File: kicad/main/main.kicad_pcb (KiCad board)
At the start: 2 copper layers, 147 parts, among them J1 USB2.0_C_v3, J10 MD2, J11 Drib, J12 SW1, J13 I2C_1, J14 drib-kick, J15 drib-kick, J16 I2C_2, J17 5V OUT, J18 LINE, J19 SW1, J2 AUX1, J20 ICSP, J21 MD1, J22 MD2, J23 MD3, J24 MD4, J25 I2C/OLED, J26 ICSP, J27 Trimmer, J3 I2C_3, J4 XBee, J5 Serial3/OpenMV, J6 Power IN, J7 LED, J8 Kicker, J9 MD1, Q1 AO3400A, Q2 AO3401A, SW1 Reset, SW2 GOAL, SW3 START, SW4 AUX1, SW5 IMU SET, SW6 RESET, SW7 BOOTSEL, U1 AZ1117CH-3.3, U10 W25Q128JVS, U2 74HC32, U3 74HC04, U4 OKL-T_3-W12N-C, U5 PCF8574PW, U6 AE-BNO055, U7 ATmega328P-AU, U8 ATmega328P-AU, U9 RP2040, Y1 8Mhz, Y2 8Mhz, Y3 12Mhz

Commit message: no message
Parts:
- removed J10: MD2, Connector_JST:JST_XH_S2B-XH-A-1_1x02_P2.50mm_Horizontal
- removed J25: I2C/OLED, 0.main.robot:JSTB4B-ZR
- removed J26: ICSP, 0.main.robot:JSTB6B-ZR
- removed J27: Trimmer, 0.main.robot:JSTS6B-ZRLFSN
- removed J7: LED, 0.main.robot:JSTB6B-ZR
- removed JP2: SolderJumper_2_Open, Jumper:SolderJumper-2_P1.3mm_Open_RoundedPad1.0x1.5mm
- removed JP3: Jumper_2_Bridged, Connector_PinHeader_1.27mm:PinHeader_1x02_P1.27mm_Vertical
- removed R49: 1kR, Resistor_SMD:R_0603_1608Metric_Pad0.98x0.95mm_HandSolder
- added C26: 0.1u, Capacitor_SMD:C_0603_1608Metric_Pad1.08x0.95mm_HandSolder, F.Cu at (170.0, 125.0)
- added C27: 10u, Capacitor_SMD:C_0603_1608Metric_Pad1.08x0.95mm_HandSolder, B.Cu at (128.0, 102.1)
- added D17: RSX101VAM-30, Diode_SMD:D_0805_2012Metric_Pad1.15x1.40mm_HandSolder, F.Cu at (142.0, 120.0)
- added D18: LED(OSWT1608), 0.main.robot:LED_SMLE13WBC8W1, F.Cu at (125.0, 103.1)
- added U11: AE-BNO055, 0.main.robot:AE-BNO055, F.Cu at (135.0, 127.0)
- C10: value 10u -> 0.1u
- C11, C12, C15, C16, C17, C22, C23, C3, C6, C8, D1, D2, D3, J1, R3, R40, SW1, U3, U4, Y2: moved to B.Cu
- C13: value 10u -> 0.1u; moved to B.Cu
- C14, C19: value 0.1u -> 1uF; moved to B.Cu
- C18, C21: value 1uF -> 0.1u; moved to B.Cu
- C24, C25: value 0.1u -> 10uF; moved to B.Cu
- C9: value 0.1u -> 10u
- D10: value RSX101VAM-30TR -> RSX101VAM-30
- D11, D12: value LED(OSWT1608) -> RSX101VAM-30; footprint LED_SMD:LED_0603_1608Metric_Pad1.05x0.95mm_HandSolder -> Diode_SMD:D_0805_2012Metric_Pad1.15x1.40mm_HandSolder; moved to B.Cu
- D13: value RSX101VAM-30TR -> LED1_R; footprint Diode_SMD:D_0805_2012Metric_Pad1.15x1.40mm_HandSolder -> 0.main.robot:LED_SMLE13WBC8W1
- D14: value LED(OSWT1608) -> LED2_G
- D15: value RSX101VAM-30 -> LED3_Y; footprint Diode_SMD:D_0805_2012Metric_Pad1.15x1.40mm_HandSolder -> 0.main.robot:LED_SMLE13WBC8W1
- D16: value RSX101VAM-30 -> LED4_B; footprint Diode_SMD:D_0805_2012Metric_Pad1.15x1.40mm_HandSolder -> 0.main.robot:LED_SMLE13WBC8W1
- D5: value LED1_R -> RSX101VAM-30TR; footprint 0.main.robot:LED_SMLE13WBC8W1 -> Diode_SMD:D_0805_2012Metric_Pad1.15x1.40mm_HandSolder
- D6: value LED2_G -> LED(OSWT1608); footprint 0.main.robot:LED_SMLE13WBC8W1 -> LED_SMD:LED_0603_1608Metric_Pad1.05x0.95mm_HandSolder
- D7: value LED3_Y -> LED(OSWT1608); footprint 0.main.robot:LED_SMLE13WBC8W1 -> LED_SMD:LED_0603_1608Metric_Pad1.05x0.95mm_HandSolder
- D8: value LED4_B -> RSX101VAM-30TR; footprint 0.main.robot:LED_SMLE13WBC8W1 -> Diode_SMD:D_0805_2012Metric_Pad1.15x1.40mm_HandSolder
- J11: value Drib -> I2C_1; footprint Connector_JST:JST_XH_B2B-XH-A_1x02_P2.50mm_Vertical -> 0.main.robot:JSTB4B-ZR
- J12: value SW1 -> drib-kick; footprint 0.main.robot:JSTB6B-ZR -> Connector_PinHeader_2.54mm:PinHeader_1x04_P2.54mm_Vertical; moved to B.Cu
- J13: value I2C_1 -> drib-kick; footprint 0.main.robot:JSTB4B-ZR -> Connector_PinHeader_2.54mm:PinHeader_1x04_P2.54mm_Vertical; moved to B.Cu
- J14: value drib-kick -> I2C_2
- J15: value drib-kick -> 5V OUT; footprint 0.main.robot:JSTB4B-ZR -> Connector_JST:JST_XH_B2B-XH-A_1x02_P2.50mm_Vertical
- J16: value I2C_2 -> LINE; footprint 0.main.robot:JSTB4B-ZR -> 0.main.robot:JSTB8B-ZR
- J17: value 5V OUT -> ICSP; footprint Connector_JST:JST_XH_B2B-XH-A_1x02_P2.50mm_Vertical -> 0.main.robot:JSTB6B-ZR
- J18: value LINE -> MD1; footprint 0.main.robot:JSTB8B-ZR -> 0.main.robot:JSTB4B-ZR
- J19: value SW1 -> MD2; footprint 0.main.robot:JSTS6B-ZRLFSN -> 0.main.robot:JSTB4B-ZR
- J20: value ICSP -> MD3; footprint 0.main.robot:JSTB6B-ZR -> 0.main.robot:JSTB4B-ZR
- J21: value MD1 -> MD4
- J22: value MD2 -> I2C/OLED
- J23: value MD3 -> ICSP; footprint 0.main.robot:JSTB4B-ZR -> 0.main.robot:JSTB6B-ZR
- J24: value MD4 -> Trimmer; footprint 0.main.robot:JSTB4B-ZR -> 0.main.robot:JSTB6B-ZR
- J4: footprint 0.main.robot:JSTB4B-ZR -> Connector_PinHeader_2.54mm:PinHeader_1x04_P2.54mm_Vertical; moved to B.Cu
- J5: value Serial3/OpenMV -> Power IN; footprint 0.main.robot:JSTB4B-ZR -> Connector_JST:JST_VH_B2P-VH-B_1x02_P3.96mm_Vertical
- J6: value Power IN -> Serial3/OpenMV; footprint Connector_JST:JST_VH_B2P-VH-B_1x02_P3.96mm_Vertical -> 0.main.robot:JSTB4B-ZR
- J8: value Kicker -> MD1; footprint Connector_JST:JST_XH_B2B-XH-A_1x02_P2.50mm_Vertical -> Connector_JST:JST_XH_S2B-XH-A-1_1x02_P2.50mm_Horizontal
- J9: value MD1 -> MD2
- JP1: value SolderJumper_2_Open -> Jumper_2_Bridged; footprint Jumper:SolderJumper-2_P1.3mm_Open_RoundedPad1.0x1.5mm -> Connector_PinHeader_1.27mm:PinHeader_1x02_P1.27mm_Vertical
- R11: value 1k -> 330
- R13: value 330 -> 10k; footprint Resistor_THT:R_Axial_DIN0204_L3.6mm_D1.6mm_P5.08mm_Horizontal -> Resistor_SMD:R_0603_1608Metric_Pad0.98x0.95mm_HandSolder
- R16, R4: value 47k -> 10k
- R17, R5, R6: value 10k -> 47k; moved to B.Cu
- R18: value 470 -> 10k; moved to B.Cu
- R19: value 470 -> 47k
- R20, R23, R28: value 47k -> 470
- R24: value 120 -> 10k
- R25, R26, R27: value 120 -> 47k; moved to B.Cu
- R29: value 47k -> 10k; moved to B.Cu
- R30: value 470 -> 1k
- R31: value 47k -> 200R
- R32: value 470 -> 1R
- R33, R34: value 47k -> 27.4R
- R35: value 470 -> 10kR; moved to B.Cu
- R36: value 10k -> 1kR
- R37: value 47k -> 470; moved to B.Cu
- R41, R7: value 10k -> 47k
- R42, R43: value 1k -> 120
- R44: value 200R -> 120
- R45: value 1R -> 120
- R46, R47: value 27.4R -> 47k; moved to B.Cu
- R48: value 10kR -> 470; moved to B.Cu
- R9: value 10k -> 1k; footprint Resistor_SMD:R_0603_1608Metric_Pad0.98x0.95mm_HandSolder -> Resistor_THT:R_Axial_DIN0204_L3.6mm_D1.6mm_P5.08mm_Horizontal
- SW2: value GOAL -> RESET; footprint 0.main.robot:MFS101D-14-Z -> 0.main.robot:TVAF06-A020B-R; moved to B.Cu
- SW3: value START -> BOOTSEL; footprint 0.main.robot:SW_NKK_B-12CCPRM -> 0.main.robot:TVAF06-A020B-R; moved to B.Cu
- SW4: value AUX1 -> IMU SET; footprint Button_Switch_THT:SW_DIP_SPSTx02_Slide_9.78x7.26mm_W7.62mm_P2.54mm -> Button_Switch_THT:SW_Tactile_Straight_KSA0Axx1LFTR
- SW5: value IMU SET -> GOAL; footprint 0.main.robot:TVAF06-A020B-R -> 0.main.robot:MFS101D-14-Z
- SW6: value RESET -> START; footprint 0.main.robot:TVAF06-A020B-R -> 0.main.robot:SW_NKK_B-12CCPRM
- SW7: value BOOTSEL -> AUX1; footprint 0.main.robot:TVAF06-A020B-R -> Button_Switch_THT:SW_DIP_SPSTx02_Slide_9.78x7.26mm_W7.62mm_P2.54mm
- U10: value W25Q128JVS -> PCF8574PW; footprint rp2040:W25Q16-128JV-SOIC -> Package_SO:TSSOP-20_4.4x6.5mm_P0.65mm; moved to B.Cu
- U5: value PCF8574PW -> ATmega328P-AU; footprint Package_SO:TSSOP-20_4.4x6.5mm_P0.65mm -> Package_QFP:TQFP-32_7x7mm_P0.8mm
- U6: value AE-BNO055 -> ATmega328P-AU; footprint 0.main.robot:AE-BNO055 -> Package_QFP:TQFP-32_7x7mm_P0.8mm
- U7: value ATmega328P-AU -> RP2040; footprint Package_QFP:TQFP-32_7x7mm_P0.8mm -> rp2040:RP2040_hand
- U8: value ATmega328P-AU -> W25Q128JVS; footprint Package_QFP:TQFP-32_7x7mm_P0.8mm -> rp2040:W25Q16-128JV-SOIC; moved to B.Cu
- U9: value RP2040 -> AZ1117CH-3.3; footprint rp2040:RP2040_hand -> Package_TO_SOT_SMD:SOT-223-3_TabPin2
- Y1, Y3: footprint Crystal:Resonator_SMD_Murata_CSTxExxV-3Pin_3.0x1.1mm_HandSoldering -> Crystal:Resonator-3Pin_W6.0mm_H3.0mm; moved to B.Cu
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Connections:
- C1 pad 2: GND -> SW1_6
- C10 pad 1: Net-(C10-Pad1) -> Vcc1
- C10 pad 2: GND -> SW1_6
- C11 pad 1: Vcc1 -> Net-(C11-Pad1)
- C11 pad 2: GND -> SW1_6
- C12 pad 1: Vcc1 -> +1V1
- C12 pad 2: GND -> SW1_6
- C13 pad 1: RESET -> +1V1
- C13 pad 2: GND -> SW1_6
- C14 pad 2: GND -> SW1_6
- C15 pad 1: +1V1 -> SW1_3
- C15 pad 2: GND -> SW1_6
- C16 pad 1: +1V1 -> SW1_3
- C16 pad 2: GND -> SW1_6
- C17 pad 1: +3V3 -> SW1_3
- C17 pad 2: GND -> SW1_6
- C18 pad 1: +3V3 -> SW1_3
- C18 pad 2: GND -> SW1_6
- C19 pad 1: +3V3 -> Net-(C19-Pad1)
- C19 pad 2: GND -> SW1_6
- C2 pad 1: +3V3 -> SW1_3
- C2 pad 2: GND -> SW1_6
- C20 pad 1: +3V3 -> SW1_3
- C20 pad 2: GND -> SW1_6
- C21 pad 1: Net-(C21-Pad1) -> SW1_3
- C21 pad 2: GND -> SW1_6
- C22 pad 1: +3V3 -> SW1_3
- C22 pad 2: GND -> SW1_6
- C23 pad 1: +3V3 -> SW1_3
- C23 pad 2: GND -> SW1_6
- C24 pad 1: +3V3 -> +5V
- C24 pad 2: GND -> SW1_6
- C25 pad 1: +3V3 -> Net-(C25-Pad1)
- C25 pad 2: GND -> SW1_6
- C3 pad 1: GND -> SW1_6
- C3 pad 2: /rp2040/RUN(RES)/30 -> RESET
- C4 pad 2: GND -> SW1_6
- C5 pad 2: Net-(C5-Pad2) -> SW1_6
- C6 pad 2: GND -> SW1_6
- C7 pad 1: +3V3 -> +3.3VA
- C7 pad 2: GND -> SW1_6
- C8 pad 1: +3V3 -> Net-(C8-Pad1)
- C8 pad 2: GND -> SW1_6
- C9 pad 1: +3.3VA -> Vcc1
- C9 pad 2: GND -> SW1_6
- D10 pad 1: +3.3VA -> RESET
- D10 pad 2: +3V3 -> Net-(C11-Pad1)
- D11 pad 1: GND -> Vcc1
- D11 pad 2: Net-(D11-Pad2) -> Net-(C11-Pad1)
- D12 pad 1: GND -> Vcc1
- D13 pad 1: +3.3VA -> Net-(D13-Pad1)
- D13 pad 2: Net-(C10-Pad1) -> Net-(D13-Pad2)
- D14 pad 1: GND -> Net-(D14-Pad1)
- D14 pad 2: Net-(D14-Pad2) -> Net-(D13-Pad2)
- D15 pad 1: Vcc1 -> Net-(D15-Pad1)
- D15 pad 2: RESET -> Net-(D13-Pad2)
- D16 pad 1: Vcc1 -> Net-(D16-Pad1)
- D16 pad 2: Net-(D16-Pad2) -> Net-(D13-Pad2)
- D3 pad 1: +3V3 -> SW1_3
- D3 pad 2: /rp2040/RUN(RES)/30 -> RESET
- D4 pad 1: GND -> SW1_6
- D5 pad 1: Net-(D5-Pad1) -> +3.3VA
- D5 pad 2: Net-(D5-Pad2) -> SW1_3
- D6 pad 1: Net-(D5-Pad1) -> SW1_6
- D7 pad 1: Net-(D5-Pad1) -> SW1_6
- D8 pad 1: Net-(D5-Pad1) -> +3.3VA
- D8 pad 2: Net-(D8-Pad2) -> Net-(C8-Pad1)
- D9 pad 1: GND -> SW1_6
- J1 pad 4: GND -> SW1_6
- J11 pad 1: +15V -> SCL_IMU
- J11 pad 2: GND -> SW1_3
- J12 pad 1: /rp2040/GPIO03/05 -> /rp2040/GPIO13/17
- J12 pad 2: /rp2040/GPIO06/09 -> SW1_6
- J12 pad 3: +3V3 -> /rp2040/GPIO12/16
- J12 pad 4: /rp2040/GPIO02/04 -> SW1_6
- J13 pad 1: SCL_IMU -> +15V
- J13 pad 2: +3V3 -> SW1_6
- J13 pad 3: SDA_IMU -> +15V
- J13 pad 4: GND -> SW1_6
- J14 pad 1: /rp2040/GPIO13/17 -> SCL_IMU
- J14 pad 2: GND -> SW1_3
- J14 pad 3: /rp2040/GPIO12/16 -> SDA_IMU
- J14 pad 4: GND -> SW1_6
- J15 pad 1: +15V -> +5V
- J15 pad 2: GND -> SW1_6
- J16 pad 1: SCL_IMU -> Net-(J16-Pad1)
- J16 pad 2: +3V3 -> Net-(J16-Pad2)
- J16 pad 3: SDA_IMU -> Net-(J16-Pad3)
- J16 pad 4: GND -> Net-(J16-Pad4)
- J17 pad 2: Net-(C5-Pad2) -> +3.3VA
- J18 pad 1: Net-(J18-Pad1) -> Net-(J17-Pad4)
- J18 pad 2: Net-(J18-Pad2) -> Net-(J17-Pad1)
- J18 pad 3: Net-(J18-Pad3) -> Net-(J17-Pad4)
- J18 pad 4: Net-(J18-Pad4) -> Net-(J17-Pad3)
- J19 pad 3: Net-(J19-Pad3) -> Net-(J19-Pad1)
- J2 pad 2: +3V3 -> SW1_3
- J2 pad 4: GND -> SW1_6
- J20 pad 2: +3.3VA -> Net-(J20-Pad2)
- J20 pad 3: Net-(J20-Pad3) -> Net-(J20-Pad1)
- J21 pad 1: Net-(J20-Pad4) -> Net-(J21-Pad1)
- J21 pad 2: Net-(J20-Pad1) -> Net-(J21-Pad2)
- J21 pad 3: Net-(J20-Pad4) -> Net-(J21-Pad1)
- J21 pad 4: Net-(J20-Pad3) -> Net-(J21-Pad4)
- J22 pad 1: Net-(J22-Pad1) -> /LineTrimmer/SCL
- J22 pad 2: Net-(J22-Pad2) -> Vcc1
- J22 pad 3: Net-(J22-Pad1) -> /LineTrimmer/SDA
- J22 pad 4: Net-(J22-Pad4) -> SW1_6
- J23 pad 2: Net-(J23-Pad2) -> Vcc1
- J23 pad 3: Net-(J23-Pad1) -> Net-(J23-Pad3)
- J24 pad 3: Net-(J24-Pad1) -> Net-(J24-Pad3)
- J3 pad 2: +3V3 -> SW1_3
- J3 pad 4: GND -> SW1_6
- J4 pad 3: /rp2040/GPIO01/02 -> Net-(J4-Pad3)
- J4 pad 4: GND -> SW1_6
- J5 pad 1: /rp2040/GPIO08/11 -> SW1_6
- J5 pad 2: +5V -> +15V
- J6 pad 1: GND -> /rp2040/GPIO08/11
- J6 pad 2: +15V -> +5V
- J8 pad 1: +15V -> SW1_6
- J8 pad 2: GND -> +15V
- J9 pad 1: GND -> SW1_6
- JP1 pad 1: Net-(JP1-Pad1) -> Net-(C25-Pad1)
- JP1 pad 2: Net-(J19-Pad5) -> Net-(D13-Pad2)
- Q1 pad 2: GND -> SW1_6
- Q2 pad 3: Net-(J18-Pad4) -> Net-(J16-Pad4)
- R1 pad 2: GND -> SW1_6
- R10 pad 2: Net-(J18-Pad6) -> Net-(J16-Pad2)
- R11 pad 1: Net-(R11-Pad1) -> SW1_6
- R12 pad 2: Net-(J18-Pad3) -> Net-(J16-Pad5)
- R13 pad 1: GND -> Net-(R13-Pad1)
- R13 pad 2: Net-(R11-Pad1) -> Net-(J16-Pad6)
- R14 pad 1: +5V -> Net-(R14-Pad1)
- R14 pad 2: Net-(Q1-Pad3) -> Net-(J16-Pad3)
- R15 pad 1: Net-(J17-Pad1) -> +5V
- R16 pad 1: +15V -> +5V
- R16 pad 2: Vbatt -> Net-(Q1-Pad3)
- R17 pad 1: Vbatt -> +15V
- R17 pad 2: GND -> Vbatt
- R18 pad 1: Net-(J19-Pad2) -> Vbatt
- R18 pad 2: Net-(R18-Pad2) -> SW1_6
- R19 pad 1: Net-(J19-Pad5) -> Net-(R19-Pad1)
- R19 pad 2: Net-(R19-Pad2) -> +3.3VA
- R2 pad 2: GND -> SW1_6
- R20 pad 1: +3V3 -> +3.3VA
- R20 pad 2: Net-(R20-Pad2) -> Net-(D6-Pad2)
- R21 pad 1: +3V3 -> +3.3VA
- R21 pad 2: Net-(R21-Pad2) -> /Sheet63625160/SCL_1
- R22 pad 1: +3V3 -> +3.3VA
- R22 pad 2: Net-(R22-Pad2) -> /Sheet63625160/SDA_1
- R23 pad 1: +3V3 -> Net-(R23-Pad1)
- R23 pad 2: Net-(R23-Pad2) -> Net-(D7-Pad2)
- R24 pad 1: Net-(R24-Pad1) -> Net-(C8-Pad1)
- R24 pad 2: Net-(D5-Pad2) -> +3.3VA
- R25 pad 2: Net-(D6-Pad2) -> Vcc1
- R26 pad 1: Net-(R26-Pad1) -> Vcc1
- R26 pad 2: Net-(D7-Pad2) -> /LineTrimmer/SCL
- R27 pad 1: Net-(JP2-Pad1) -> Vcc1
- R27 pad 2: Net-(D8-Pad2) -> /LineTrimmer/SDA
- R28 pad 1: +3V3 -> Net-(R28-Pad1)
- R28 pad 2: SDA_IMU -> Net-(D9-Pad2)
- R29 pad 1: +3V3 -> Net-(C11-Pad1)
- R29 pad 2: SCL_IMU -> Vcc1
- R3 pad 1: /rp2040/GPIO09/12 -> /rp2040/GPIO01/02
- R3 pad 2: Net-(J5-Pad3) -> Net-(J4-Pad3)
- R30 pad 1: +3V3 -> Net-(R30-Pad1)
- R30 pad 2: Net-(D9-Pad2) -> Net-(R30-Pad2)
- R31 pad 1: Net-(R31-Pad1) -> ADC_VREF
- R31 pad 2: +3.3VA -> SW1_3
- R32 pad 1: +3.3VA -> Net-(C19-Pad1)
- R32 pad 2: Net-(D11-Pad2) -> ADC_VREF
- R33 pad 1: +3.3VA -> Net-(R33-Pad1)
- R33 pad 2: /Sheet63625160/SCL_1 -> USB_DP
- R34 pad 1: +3.3VA -> Net-(R34-Pad1)
- R34 pad 2: /Sheet63625160/SDA_1 -> USB_DM
- R35 pad 1: Net-(R35-Pad1) -> QSPI_SS
- R35 pad 2: Net-(D12-Pad2) -> SW1_3
- R36 pad 1: Net-(C10-Pad1) -> Net-(R36-Pad1)
- R36 pad 2: +3.3VA -> QSPI_SS
- R37 pad 2: Vcc1 -> Net-(R37-Pad2)
- R38 pad 1: Vcc1 -> Net-(C25-Pad1)
- R38 pad 2: /LineTrimmer/SCL -> Net-(R38-Pad2)
- R39 pad 1: Vcc1 -> Net-(C25-Pad1)
- R39 pad 2: /LineTrimmer/SDA -> Net-(R39-Pad2)
- R4 pad 1: +3V3 -> /rp2040/GPIO09/12
- R4 pad 2: /rp2040/RUN(RES)/30 -> Net-(J6-Pad3)
- R40 pad 2: Net-(D14-Pad2) -> Net-(R40-Pad2)
- R41 pad 1: RESET -> Net-(C25-Pad1)
- R41 pad 2: Vcc1 -> Net-(R41-Pad2)
- R42 pad 1: /rp2040/RUN(RES)/30 -> Net-(R42-Pad1)
- R42 pad 2: +3V3 -> Net-(D13-Pad1)
- R43 pad 2: Net-(R43-Pad2) -> Net-(D14-Pad1)
- R44 pad 1: ADC_VREF -> Net-(R44-Pad1)
- R44 pad 2: +3V3 -> Net-(D15-Pad1)
- R45 pad 1: Net-(C21-Pad1) -> Net-(R45-Pad1)
- R45 pad 2: ADC_VREF -> Net-(D16-Pad1)
- R46 pad 1: Net-(R46-Pad1) -> Net-(C25-Pad1)
- R46 pad 2: USB_DP -> SDA_IMU
- R47 pad 1: Net-(R47-Pad1) -> Net-(C25-Pad1)
- R47 pad 2: USB_DM -> SCL_IMU
- R48 pad 1: QSPI_SS -> Net-(C25-Pad1)
- R48 pad 2: +3V3 -> Net-(D18-Pad2)
- R5 pad 1: +3V3 -> SW1_3
- R5 pad 2: SCL_IMU -> RESET
- R6 pad 1: +3V3 -> SW1_3
- R6 pad 2: SDA_IMU -> SCL_IMU
- R7 pad 1: Net-(R7-Pad1) -> SW1_3
- R7 pad 2: Net-(J18-Pad1) -> SDA_IMU
- R8 pad 2: Net-(J18-Pad2) -> Net-(J16-Pad1)
- R9 pad 1: Net-(R9-Pad1) -> Net-(R11-Pad2)
- R9 pad 2: Net-(J18-Pad5) -> Net-(R9-Pad2)
- RV1 pad 1: Net-(D16-Pad2) -> Net-(D12-Pad2)
- RV1 pad 2: Net-(J27-Pad1) -> Net-(J24-Pad1)
- RV1 pad 3: Net-(J27-Pad1) -> Net-(J24-Pad1)
- RV2 pad 1: Net-(D16-Pad2) -> Net-(D12-Pad2)
- RV2 pad 2: Net-(J27-Pad2) -> Net-(J24-Pad2)
- RV2 pad 3: Net-(J27-Pad2) -> Net-(J24-Pad2)
- RV3 pad 1: Net-(D16-Pad2) -> Net-(D12-Pad2)
- RV3 pad 2: Net-(J27-Pad3) -> Net-(J24-Pad3)
- RV3 pad 3: Net-(J27-Pad3) -> Net-(J24-Pad3)
- RV4 pad 1: Net-(D16-Pad2) -> Net-(D12-Pad2)
- RV4 pad 2: Net-(J27-Pad4) -> Net-(J24-Pad4)
- RV4 pad 3: Net-(J27-Pad4) -> Net-(J24-Pad4)
- RV5 pad 1: Net-(D16-Pad2) -> Net-(D12-Pad2)
- SW1 pad 1: /rp2040/RUN(RES)/30 -> RESET
- SW1 pad 2: GND -> SW1_6
- SW2 pad 1: Net-(J19-Pad3) -> SW1_6
- SW2 pad 2: Net-(J19-Pad1) -> Net-(C11-Pad1)
- SW3 pad 1: Net-(J19-Pad3) -> SW1_6
- SW3 pad 2: Net-(J19-Pad4) -> Net-(R36-Pad1)
- SW4 pad 1: GND -> SW1_5
- SW4 pad 2: GND -> SW1_6
- SW5 pad 1: Net-(R22-Pad2) -> SW1_3
- SW5 pad 2: GND -> SW1_1
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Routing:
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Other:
- board outline added: 169.8 x 107.5 mm

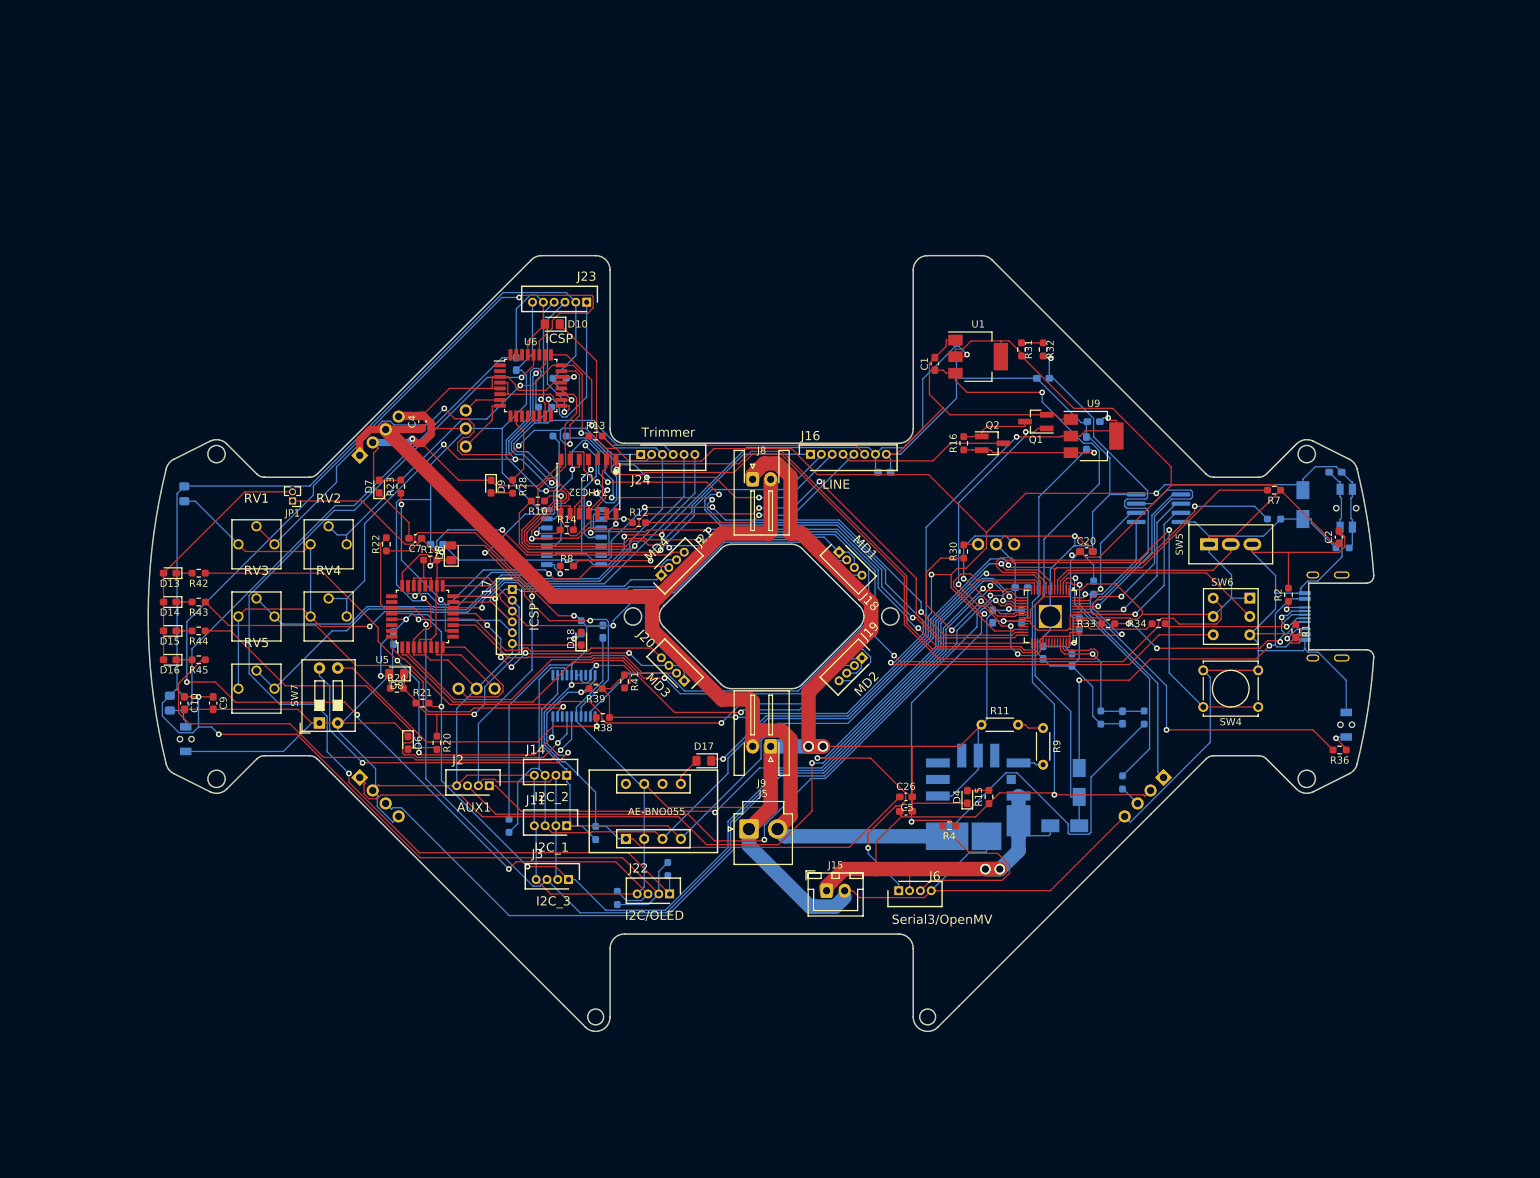
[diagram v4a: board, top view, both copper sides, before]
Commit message: fix: vison-board GND
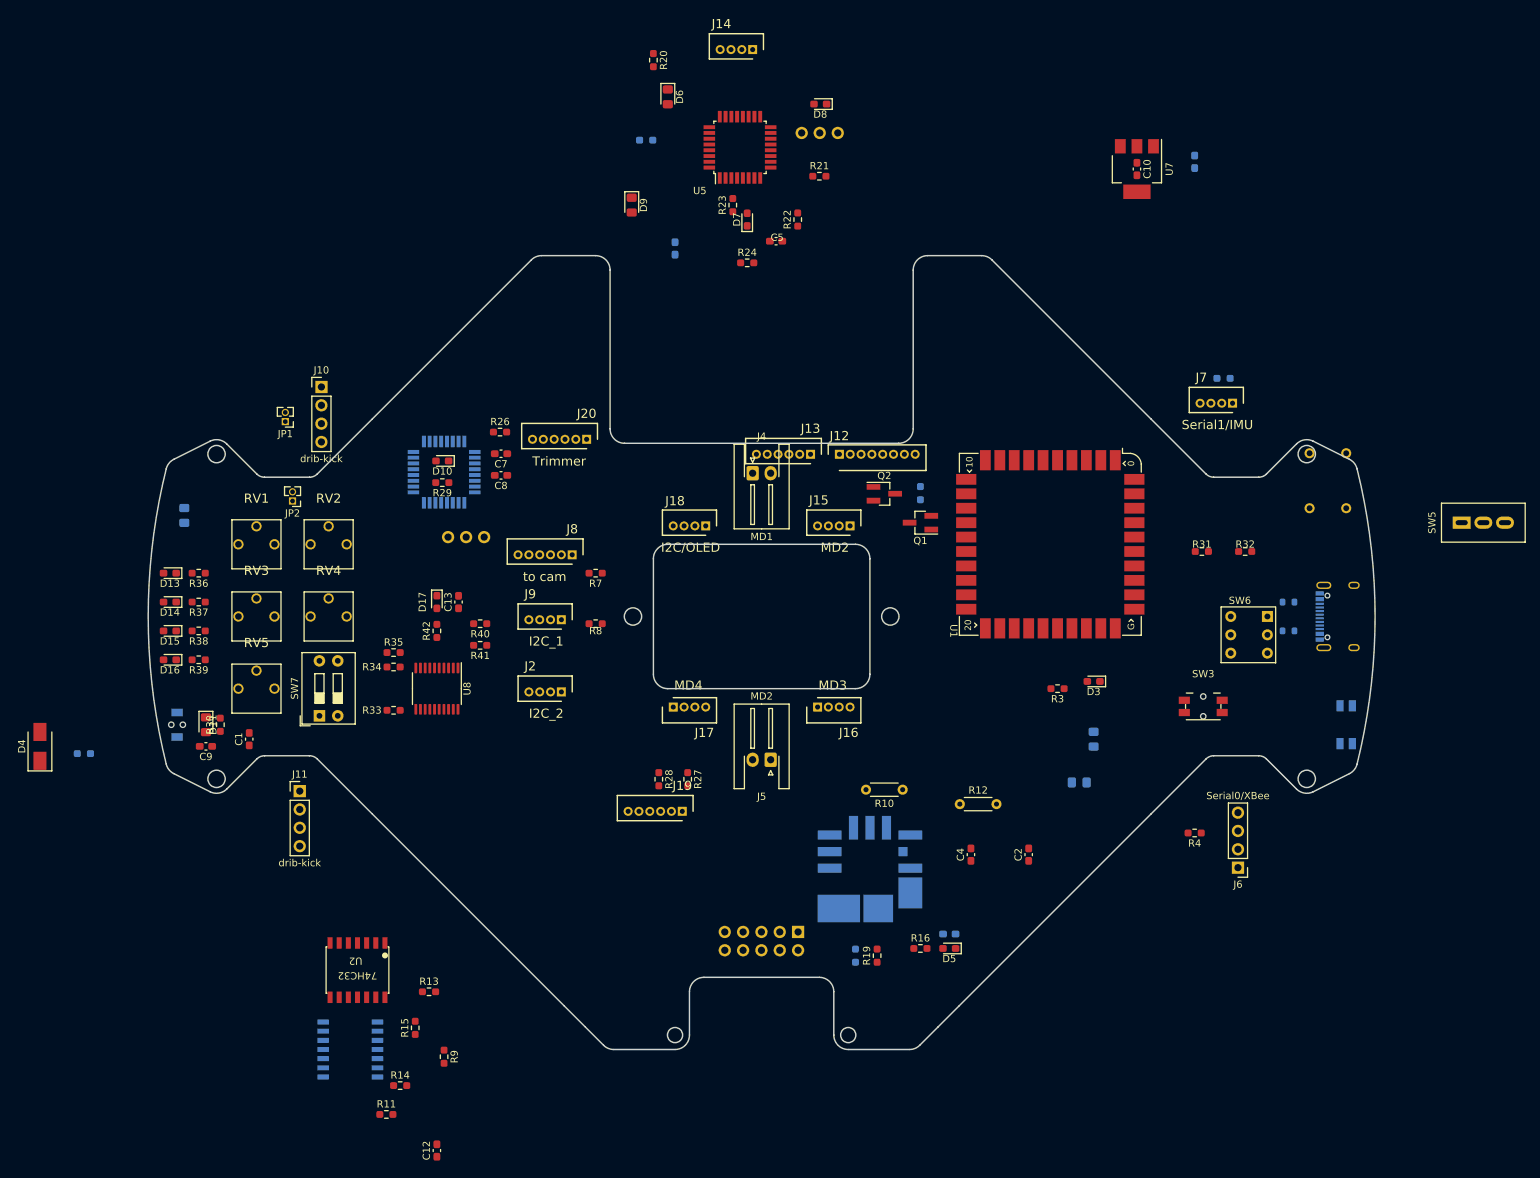
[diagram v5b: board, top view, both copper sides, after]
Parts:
- removed C14, C16, C19: 1uF, Capacitor_SMD:C_0603_1608Metric_Pad1.08x0.95mm_HandSolder
- removed C15, C17, C18, C20, C21, C22, C23, C26: 0.1u, Capacitor_SMD:C_0603_1608Metric_Pad1.08x0.95mm_HandSolder
- removed C24, C25: 10uF, Capacitor_SMD:C_0603_1608Metric_Pad1.08x0.95mm_HandSolder
- removed C27: 10u, Capacitor_SMD:C_0603_1608Metric_Pad1.08x0.95mm_HandSolder
- removed D18: LED(OSWT1608), 0.main.robot:LED_SMLE13WBC8W1
- removed J21: MD4, 0.main.robot:JSTB4B-ZR
- removed J22: I2C/OLED, 0.main.robot:JSTB4B-ZR
- removed J23: ICSP, 0.main.robot:JSTB6B-ZR
- removed J24: Trimmer, 0.main.robot:JSTB6B-ZR
- removed R43, R44, R45: 120, Resistor_SMD:R_0603_1608Metric_Pad0.98x0.95mm_HandSolder
- removed R46, R47: 47k, Resistor_SMD:R_0603_1608Metric_Pad0.98x0.95mm_HandSolder
- removed R48: 470, Resistor_SMD:R_0603_1608Metric_Pad0.98x0.95mm_HandSolder
- removed U10: PCF8574PW, Package_SO:TSSOP-20_4.4x6.5mm_P0.65mm
- removed U11: AE-BNO055, 0.main.robot:AE-BNO055
- removed U9: AZ1117CH-3.3, Package_TO_SOT_SMD:SOT-223-3_TabPin2
- removed Y3: 12Mhz, Crystal:Resonator-3Pin_W6.0mm_H3.0mm
- added J10: drib-kick, Connector_PinHeader_2.54mm:PinHeader_1x04_P2.54mm_Vertical, F.Cu at (89.0, 68.2)
- added J7: Serial1/IMU, 0.main.robot:JSTB4B-ZR, F.Cu at (215.2, 70.5)
- added JP2: Jumper_2_Bridged, Connector_PinHeader_1.27mm:PinHeader_1x02_P1.27mm_Vertical, F.Cu at (85.0, 84.0)
- C1, C2: value 10uF -> 10u
- C10: value 0.1u -> 10uF
- C11: value 10u -> 10uF
- C12, D11, R26: moved to F.Cu
- C13: value 0.1u -> 10u; moved to F.Cu
- C5: value 10u -> 0.1u
- C7: value 0.1u -> 10u
- C8: value 10u -> 0.1u; moved to F.Cu
- D1, D2: value SX34F -> D_Schottky; footprint Diode_SMD:D_SMA -> Diode_SMD:D_0805_2012Metric_Pad1.15x1.40mm_HandSolder
- D10, D17: value RSX101VAM-30 -> LED(OSWT1608); footprint Diode_SMD:D_0805_2012Metric_Pad1.15x1.40mm_HandSolder -> 0.main.robot:LED_SMLE13WBC8W1
- D3: value RSX101VAM-30TR -> LED; footprint Diode_SMD:D_SMA -> 0.main.robot:LED_SMLE13WBC8W1; moved to F.Cu
- D4: value LED -> RSX101VAM-30TR; footprint 0.main.robot:LED_SMLE13WBC8W1 -> Diode_SMD:D_SMA
- D5: value RSX101VAM-30TR -> LED; footprint Diode_SMD:D_0805_2012Metric_Pad1.15x1.40mm_HandSolder -> 0.main.robot:LED_SMLE13WBC8W1
- D6: value LED(OSWT1608) -> RSX101VAM-30TR; footprint LED_SMD:LED_0603_1608Metric_Pad1.05x0.95mm_HandSolder -> Diode_SMD:D_0805_2012Metric_Pad1.15x1.40mm_HandSolder
- D8: value RSX101VAM-30TR -> LED(OSWT1608); footprint Diode_SMD:D_0805_2012Metric_Pad1.15x1.40mm_HandSolder -> LED_SMD:LED_0603_1608Metric_Pad1.05x0.95mm_HandSolder
- D9: value LED(OSWT1608) -> RSX101VAM-30TR; footprint 0.main.robot:LED_SMLE13WBC8W1 -> Diode_SMD:D_0805_2012Metric_Pad1.15x1.40mm_HandSolder
- J1: value USB2.0_C_v3 -> USB_C_Receptacle_USB2.0; footprint rp2040:USB-C-12-Pin-MidMount-ali-v4 -> Connector_USB:USB_C_Receptacle_XKB_U262-16XN-4BVC11
- J11: value I2C_1 -> drib-kick; footprint 0.main.robot:JSTB4B-ZR -> Connector_PinHeader_2.54mm:PinHeader_1x04_P2.54mm_Vertical
- J12: value drib-kick -> LINE; footprint Connector_PinHeader_2.54mm:PinHeader_1x04_P2.54mm_Vertical -> 0.main.robot:JSTB8B-ZR; moved to F.Cu
- J13: value drib-kick -> ICSP; footprint Connector_PinHeader_2.54mm:PinHeader_1x04_P2.54mm_Vertical -> 0.main.robot:JSTB6B-ZR; moved to F.Cu
- J14: value I2C_2 -> MD1
- J15: value 5V OUT -> MD2; footprint Connector_JST:JST_XH_B2B-XH-A_1x02_P2.50mm_Vertical -> 0.main.robot:JSTB4B-ZR
- J16: value LINE -> MD3; footprint 0.main.robot:JSTB8B-ZR -> 0.main.robot:JSTB4B-ZR
- J17: value ICSP -> MD4; footprint 0.main.robot:JSTB6B-ZR -> 0.main.robot:JSTB4B-ZR
- J18: value MD1 -> I2C/OLED
- J19: value MD2 -> ICSP; footprint 0.main.robot:JSTB4B-ZR -> 0.main.robot:JSTB6B-ZR
- J2: value AUX1 -> I2C_2
- J20: value MD3 -> Trimmer; footprint 0.main.robot:JSTB4B-ZR -> 0.main.robot:JSTB6B-ZR
- J3: value I2C_3 -> Power IN; footprint 0.main.robot:JSTB4B-ZR -> Connector_PinSocket_2.54mm:PinSocket_2x05_P2.54mm_Vertical; moved to B.Cu
- J4: value XBee -> MD1; footprint Connector_PinHeader_2.54mm:PinHeader_1x04_P2.54mm_Vertical -> Connector_JST:JST_XH_S2B-XH-A-1_1x02_P2.50mm_Horizontal; moved to F.Cu
- J5: value Power IN -> MD2; footprint Connector_JST:JST_VH_B2P-VH-B_1x02_P3.96mm_Vertical -> Connector_JST:JST_XH_S2B-XH-A-1_1x02_P2.50mm_Horizontal
- J6: value Serial3/OpenMV -> Serial0/XBee; footprint 0.main.robot:JSTB4B-ZR -> Connector_PinHeader_2.54mm:PinHeader_1x04_P2.54mm_Vertical
- J8: value MD1 -> to cam; footprint Connector_JST:JST_XH_S2B-XH-A-1_1x02_P2.50mm_Horizontal -> 0.main.robot:JSTB6B-ZR
- J9: value MD2 -> I2C_1; footprint Connector_JST:JST_XH_S2B-XH-A-1_1x02_P2.50mm_Horizontal -> 0.main.robot:JSTB4B-ZR
- R1, R2: value 5.1kR -> 5.1K; footprint Resistor_SMD:R_0603_1608Metric_Pad0.98x0.95mm_HandSolder -> Resistor_SMD:R_0603_1608Metric; moved to B.Cu
- R10: value 10k -> 1k; footprint Resistor_SMD:R_0603_1608Metric_Pad0.98x0.95mm_HandSolder -> Resistor_THT:R_Axial_DIN0204_L3.6mm_D1.6mm_P5.08mm_Horizontal
- R11: value 330 -> 10k; footprint Resistor_THT:R_Axial_DIN0204_L3.6mm_D1.6mm_P5.08mm_Horizontal -> Resistor_SMD:R_0603_1608Metric_Pad0.98x0.95mm_HandSolder
- R12: value 10k -> 330; footprint Resistor_SMD:R_0603_1608Metric_Pad0.98x0.95mm_HandSolder -> Resistor_THT:R_Axial_DIN0204_L3.6mm_D1.6mm_P5.08mm_Horizontal
- R15, R23, R28: value 470 -> 10k
- R16, R24: value 10k -> 470
- R17, R19, R22, R25, R6: value 47k -> 10k
- R18, R8: value 10k -> 47k
- R20: value 470 -> 47k
- R21: value 47k -> 470
- R27: value 47k -> 10k; moved to F.Cu
- R29, R3: value 10k -> 470; moved to F.Cu
- R30: value 1k -> 10k
- R31: value 200R -> 120
- R32: value 1R -> 120
- R33, R34: value 27.4R -> 47k
- R35: value 10kR -> 47k; moved to F.Cu
- R36: value 1kR -> 120
- R37: value 470 -> 120; moved to F.Cu
- R38, R39: value 47k -> 120
- R40: value 470 -> 47k; moved to F.Cu
- R42: value 120 -> 470
- R9: value 1k -> 10k; footprint Resistor_THT:R_Axial_DIN0204_L3.6mm_D1.6mm_P5.08mm_Horizontal -> Resistor_SMD:R_0603_1608Metric_Pad0.98x0.95mm_HandSolder
- SW1: value Reset -> BOOTSET; footprint 0.main.robot:THAU13-AB-R -> Button_Switch_SMD:Panasonic_EVQPUJ_EVQPUA
- SW2: value RESET -> IMU SET; footprint 0.main.robot:TVAF06-A020B-R -> Button_Switch_THT:SW_Tactile_Straight_KSA0Axx1LFTR
- SW3: value BOOTSEL -> Reset; footprint 0.main.robot:TVAF06-A020B-R -> 0.main.robot:THAU13-AB-R; moved to F.Cu
- SW4: value IMU SET -> RESET; footprint Button_Switch_THT:SW_Tactile_Straight_KSA0Axx1LFTR -> 0.main.robot:TVAF06-A020B-R; moved to B.Cu
- U1: value AZ1117CH-3.3 -> RP2040_Stamp; footprint Package_TO_SOT_SMD:SOT-223-3_TabPin2 -> rp2040_stamp:RP2040_Stamp_SMD
- U6: moved to B.Cu
- U7: value RP2040 -> AZ1117CH-3.3; footprint rp2040:RP2040_hand -> Package_TO_SOT_SMD:SOT-223-3_TabPin2
- U8: value W25Q128JVS -> PCF8574PW; footprint rp2040:W25Q16-128JV-SOIC -> Package_SO:TSSOP-20_4.4x6.5mm_P0.65mm; moved to F.Cu
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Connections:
- C1 pad 1: Net-(C1-Pad1) -> SW1_6
- C1 pad 2: SW1_6 -> /RESET
- C10 pad 1: Vcc1 -> +5V
- C12 pad 1: +1V1 -> Net-(C11-Pad1)
- C13 pad 1: +1V1 -> Net-(C11-Pad1)
- C2 pad 1: SW1_3 -> +15V
- C3 pad 1: SW1_6 -> +5V
- C3 pad 2: RESET -> SW1_6
- C4 pad 1: +15V -> Vbatt
- C5 pad 1: +5V -> +3.3VA
- C6 pad 1: Vbatt -> Net-(C6-Pad1)
- C7 pad 1: +3.3VA -> Vcc1
- C8 pad 1: Net-(C8-Pad1) -> Vcc1
- C9 pad 1: Vcc1 -> Net-(C9-Pad1)
- D1 pad 1: Net-(C1-Pad1) -> Net-(D1-Pad1)
- D1 pad 2: Net-(D1-Pad2) -> VBUS
- D10 pad 1: RESET -> SW1_6
- D10 pad 2: Net-(C11-Pad1) -> Net-(D10-Pad2)
- D11 pad 2: Net-(C11-Pad1) -> Net-(C9-Pad1)
- D17 pad 1: RESET -> SW1_6
- D2 pad 1: Net-(C1-Pad1) -> Net-(D1-Pad1)
- D3 pad 1: SW1_3 -> SW1_6
- D3 pad 2: RESET -> Net-(D3-Pad2)
- D4 pad 1: SW1_6 -> SW1_3
- D4 pad 2: Net-(D4-Pad2) -> /RESET
- D5 pad 1: +3.3VA -> SW1_6
- D5 pad 2: SW1_3 -> Net-(D5-Pad2)
- D6 pad 1: SW1_6 -> +3.3VA
- D6 pad 2: Net-(D6-Pad2) -> SW1_3
- D8 pad 1: +3.3VA -> SW1_6
- D8 pad 2: Net-(C8-Pad1) -> Net-(D8-Pad2)
- D9 pad 1: SW1_6 -> +3.3VA
- D9 pad 2: Net-(D9-Pad2) -> Net-(C6-Pad1)
- J11 pad 1: SCL_IMU -> +15V
- J11 pad 2: SW1_3 -> SW1_6
- J11 pad 3: SDA_IMU -> +15V
- J12 pad 1: /rp2040/GPIO13/17 -> Net-(J12-Pad1)
- J12 pad 2: SW1_6 -> Net-(J12-Pad2)
- J12 pad 3: /rp2040/GPIO12/16 -> Net-(J12-Pad3)
- J12 pad 4: SW1_6 -> Net-(J12-Pad4)
- J13 pad 1: +15V -> Net-(J13-Pad1)
- J13 pad 2: SW1_6 -> +3.3VA
- J13 pad 3: +15V -> Net-(J13-Pad3)
- J13 pad 4: SW1_6 -> Net-(J13-Pad4)
- J14 pad 1: SCL_IMU -> Net-(J13-Pad4)
- J14 pad 2: SW1_3 -> Net-(J13-Pad1)
- J14 pad 3: SDA_IMU -> Net-(J13-Pad4)
- J14 pad 4: SW1_6 -> Net-(J13-Pad3)
- J15 pad 1: +5V -> Net-(J15-Pad1)
- J15 pad 2: SW1_6 -> Net-(J15-Pad2)
- J16 pad 3: Net-(J16-Pad3) -> Net-(J16-Pad1)
- J17 pad 2: +3.3VA -> Net-(J17-Pad2)
- J17 pad 3: Net-(J17-Pad3) -> Net-(J17-Pad1)
- J18 pad 1: Net-(J17-Pad4) -> /LineTrimmer/SCL
- J18 pad 2: Net-(J17-Pad1) -> Vcc1
- J18 pad 3: Net-(J17-Pad4) -> /LineTrimmer/SDA
- J18 pad 4: Net-(J17-Pad3) -> SW1_6
- J19 pad 2: Net-(J19-Pad2) -> Vcc1
- J19 pad 3: Net-(J19-Pad1) -> Net-(J19-Pad3)
- J2 pad 1: /rp2040/GPIO14/19 -> I2C_1.SCL
- J2 pad 3: /rp2040/GPIO15/20 -> I2C_1.SDA
- J20 pad 3: Net-(J20-Pad1) -> Net-(J20-Pad3)
- J3 pad 1: /Sheet63625160/SCL_1 -> SW1_6
- J3 pad 2: SW1_3 -> +15V
- J3 pad 3: /Sheet63625160/SDA_1 -> SW1_6
- J3 pad 4: SW1_6 -> +15V
- J4 pad 1: /rp2040/GPIO00/01 -> SW1_6
- J4 pad 2: +5V -> +15V
- J6 pad 1: /rp2040/GPIO08/11 -> Net-(J6-Pad1)
- J8 pad 1: SW1_6 -> I2C_0.SCL
- J8 pad 2: +15V -> +5V
- J9 pad 1: SW1_6 -> I2C_0.SCL
- J9 pad 2: +15V -> SW1_3
- JP1 pad 1: Net-(C25-Pad1) -> SW1_6
- JP1 pad 2: Net-(D13-Pad2) -> Net-(J10-Pad2)
- Q1 pad 1: /rp2040/GPIO21/27 -> Net-(Q1-Pad1)
- Q2 pad 3: Net-(J16-Pad4) -> Net-(J12-Pad4)
- R1 pad 1: Net-(J1-Pad6) -> Net-(J1-PadA5)
- R10 pad 2: Net-(J16-Pad2) -> Net-(R10-Pad2)
- R11 pad 1: SW1_6 -> Net-(R11-Pad1)
- R11 pad 2: Net-(R11-Pad2) -> Net-(J12-Pad2)
- R12 pad 1: Net-(R12-Pad1) -> SW1_6
- R12 pad 2: Net-(J16-Pad5) -> Net-(R10-Pad1)
- R13 pad 2: Net-(J16-Pad6) -> Net-(J12-Pad5)
- R14 pad 2: Net-(J16-Pad3) -> Net-(J12-Pad6)
- R15 pad 1: +5V -> Net-(R15-Pad1)
- R15 pad 2: Net-(D4-Pad2) -> Net-(J12-Pad3)
- R16 pad 2: Net-(Q1-Pad3) -> Net-(D5-Pad2)
- R17 pad 1: +15V -> +5V
- R17 pad 2: Vbatt -> Net-(Q1-Pad3)
- R18 pad 1: Vbatt -> +15V
- R18 pad 2: SW1_6 -> Vbatt
- R19 pad 1: Net-(R19-Pad1) -> Vbatt
- R19 pad 2: +3.3VA -> SW1_6
- R2 pad 1: Net-(J1-Pad5) -> Net-(J1-PadB5)
- R20 pad 1: +3.3VA -> Net-(R20-Pad1)
- R20 pad 2: Net-(D6-Pad2) -> +3.3VA
- R21 pad 2: /Sheet63625160/SCL_1 -> Net-(D7-Pad2)
- R22 pad 2: /Sheet63625160/SDA_1 -> I2C_1.SCL
- R23 pad 1: Net-(R23-Pad1) -> +3.3VA
- R23 pad 2: Net-(D7-Pad2) -> I2C_1.SDA
- R24 pad 1: Net-(C8-Pad1) -> Net-(R24-Pad1)
- R24 pad 2: +3.3VA -> Net-(D8-Pad2)
- R25 pad 1: Net-(R25-Pad1) -> Net-(C6-Pad1)
- R25 pad 2: Vcc1 -> +3.3VA
- R26 pad 1: Vcc1 -> Net-(R26-Pad1)
- R26 pad 2: /LineTrimmer/SCL -> Vcc1
- R27 pad 2: /LineTrimmer/SDA -> /LineTrimmer/SCL
- R28 pad 1: Net-(R28-Pad1) -> Vcc1
- R28 pad 2: Net-(D9-Pad2) -> /LineTrimmer/SDA
- R29 pad 1: Net-(C11-Pad1) -> Net-(R29-Pad1)
- R29 pad 2: Vcc1 -> Net-(D10-Pad2)
- R3 pad 1: /rp2040/GPIO01/02 -> Net-(D3-Pad2)
- R3 pad 2: Net-(J4-Pad3) -> Net-(R3-Pad2)
- R30 pad 1: Net-(R30-Pad1) -> Net-(C9-Pad1)
- R30 pad 2: Net-(R30-Pad2) -> Vcc1
- R31 pad 1: ADC_VREF -> SW1_2
- R31 pad 2: SW1_3 -> Net-(R31-Pad2)
- R32 pad 1: Net-(C19-Pad1) -> Net-(R32-Pad1)
- R32 pad 2: ADC_VREF -> SW1_5
- R33 pad 1: Net-(R33-Pad1) -> Net-(C11-Pad1)
- R33 pad 2: USB_DP -> Net-(R33-Pad2)
- R34 pad 1: Net-(R34-Pad1) -> Net-(C11-Pad1)
- R34 pad 2: USB_DM -> Net-(R34-Pad2)
- R35 pad 1: QSPI_SS -> Net-(C11-Pad1)
- R35 pad 2: SW1_3 -> Net-(R35-Pad2)
- R36 pad 2: QSPI_SS -> Net-(D13-Pad1)
- R37 pad 2: Net-(R37-Pad2) -> Net-(D14-Pad1)
- R38 pad 1: Net-(C25-Pad1) -> Net-(R38-Pad1)
- R38 pad 2: Net-(R38-Pad2) -> Net-(D15-Pad1)
- R39 pad 1: Net-(C25-Pad1) -> Net-(R39-Pad1)
- R39 pad 2: Net-(R39-Pad2) -> Net-(D16-Pad1)
- R4 pad 1: /rp2040/GPIO09/12 -> Net-(J6-Pad3)
- R4 pad 2: Net-(J6-Pad3) -> Net-(R4-Pad2)
- R40 pad 1: Net-(R40-Pad1) -> Net-(C11-Pad1)
- R40 pad 2: Net-(R40-Pad2) -> I2C_1.SDA
- R41 pad 1: Net-(C25-Pad1) -> Net-(C11-Pad1)
- R41 pad 2: Net-(R41-Pad2) -> I2C_1.SCL
- R42 pad 1: Net-(R42-Pad1) -> Net-(C11-Pad1)
- R42 pad 2: Net-(D13-Pad1) -> Net-(D17-Pad2)
- R5 pad 2: RESET -> /RESET
- R6 pad 1: SW1_3 -> Net-(R6-Pad1)
- R6 pad 2: SCL_IMU -> Net-(J7-Pad3)
- R7 pad 2: SDA_IMU -> I2C_0.SCL
- R8 pad 1: Net-(R8-Pad1) -> SW1_3
- R8 pad 2: Net-(J16-Pad1) -> I2C_0.SDA
- R9 pad 1: Net-(R11-Pad2) -> Net-(R9-Pad1)
- R9 pad 2: Net-(R9-Pad2) -> Net-(J12-Pad1)
- RV1 pad 2: Net-(J24-Pad1) -> Net-(J20-Pad1)
- RV1 pad 3: Net-(J24-Pad1) -> Net-(J20-Pad1)
- RV2 pad 2: Net-(J24-Pad2) -> Net-(J20-Pad2)
- RV2 pad 3: Net-(J24-Pad2) -> Net-(J20-Pad2)
- RV3 pad 2: Net-(J24-Pad3) -> Net-(J20-Pad3)
- RV3 pad 3: Net-(J24-Pad3) -> Net-(J20-Pad3)
- RV4 pad 2: Net-(J24-Pad4) -> Net-(J20-Pad4)
- RV4 pad 3: Net-(J24-Pad4) -> Net-(J20-Pad4)
- SW1 pad 1: RESET -> SW1_6
- SW1 pad 2: SW1_6 -> /BOOTSET
- SW2 pad 2: Net-(C11-Pad1) -> IMU SET
- SW3 pad 1: SW1_6 -> /RESET
- SW3 pad 2: Net-(R36-Pad1) -> SW1_6
- SW4 pad 1: SW1_5 -> SW1_6
- SW4 pad 2: SW1_6 -> Net-(C9-Pad1)
- SW6 pad 4: Net-(R37-Pad1) -> Net-(R31-Pad2)
- SW6 pad 6: Net-(R40-Pad1) -> Net-(R32-Pad1)
- SW7 pad 3: Net-(R38-Pad2) -> Net-(R33-Pad2)
- SW7 pad 4: Net-(R39-Pad2) -> Net-(R34-Pad2)
- U1 pad 1: SW1_6 -> Net-(J6-Pad1)
- U1 pad 2: SW1_3 -> Net-(R4-Pad2)
- U1 pad 3: Net-(C1-Pad1) -> SW1_4
- U2 pad 1: /rp2040/GPIO20/26 -> LINE_D_5
- U2 pad 10: /rp2040/GPIO19/25 -> LINE_D_4
- U2 pad 3: /rp2040/GPIO28/34 -> LINE_D_6
- U2 pad 4: /rp2040/GPIO16/21 -> LINE_D_1
- U2 pad 5: /rp2040/GPIO18/24 -> LINE_D_3
- U2 pad 9: /rp2040/GPIO17/22 -> LINE_D_2
- U3 pad 1: Net-(R8-Pad1) -> Net-(R9-Pad1)
- U3 pad 10: /rp2040/GPIO20/26 -> LINE_D_5
- U3 pad 11: Net-(R13-Pad1) -> Net-(R14-Pad1)
- U3 pad 2: /rp2040/GPIO16/21 -> LINE_D_1
- U3 pad 3: Net-(R10-Pad1) -> Net-(R11-Pad1)
- U3 pad 4: /rp2040/GPIO17/22 -> LINE_D_2
- U3 pad 5: Net-(R14-Pad1) -> Net-(R15-Pad1)
- U3 pad 6: /rp2040/GPIO18/24 -> LINE_D_3
- U3 pad 8: /rp2040/GPIO19/25 -> LINE_D_4
- U3 pad 9: Net-(R12-Pad1) -> Net-(R13-Pad1)
- U4 pad 6: Net-(R9-Pad2) -> Net-(R10-Pad2)
- U5 pad 1: Net-(J19-Pad2) -> Net-(J15-Pad1)
- U5 pad 10: Net-(R23-Pad1) -> Net-(R24-Pad1)
- U5 pad 11: Net-(J20-Pad2) -> Net-(J16-Pad2)
- U5 pad 12: Net-(J20-Pad4) -> Net-(J16-Pad4)
- U5 pad 13: Net-(J20-Pad1) -> Net-(J16-Pad1)
- U5 pad 14: Net-(J21-Pad1) -> Net-(J17-Pad1)
- U5 pad 15: Net-(J17-Pad4) -> Net-(J13-Pad4)
- U5 pad 16: Net-(J17-Pad1) -> Net-(J13-Pad1)
- U5 pad 17: Net-(J17-Pad3) -> Net-(J13-Pad3)
- U5 pad 19: Net-(R19-Pad1) -> Net-(R20-Pad1)
- U5 pad 2: Net-(J19-Pad4) -> Net-(J15-Pad4)
- U5 pad 22: Net-(R19-Pad1) -> Net-(R20-Pad1)
- U5 pad 23: Net-(J21-Pad2) -> Net-(J17-Pad2)
- U5 pad 24: Net-(J21-Pad4) -> Net-(J17-Pad4)
- U5 pad 27: /Sheet63625160/SDA_1 -> I2C_1.SDA
- U5 pad 28: /Sheet63625160/SCL_1 -> I2C_1.SCL
- U5 pad 29: Net-(C8-Pad1) -> Net-(C6-Pad1)
- U5 pad 32: Net-(J19-Pad1) -> Net-(J15-Pad2)
- U6 pad 1: unconnected-(U6-Pad1) -> LINE_D_4
- U6 pad 10: Net-(R28-Pad1) -> Net-(R29-Pad1)
- U6 pad 15: Net-(J23-Pad4) -> Net-(J19-Pad4)
- U6 pad 16: Net-(J23-Pad1) -> Net-(J19-Pad1)
- U6 pad 17: Net-(J23-Pad3) -> Net-(J19-Pad3)
- U6 pad 2: unconnected-(U6-Pad2) -> LINE_D_5
- U6 pad 22: Net-(R25-Pad1) -> Net-(R26-Pad1)
- U6 pad 23: Net-(J24-Pad1) -> Net-(J20-Pad1)
- U6 pad 24: Net-(J24-Pad2) -> Net-(J20-Pad2)
- U6 pad 25: Net-(J24-Pad3) -> Net-(J20-Pad3)
- U6 pad 26: Net-(J24-Pad4) -> Net-(J20-Pad4)
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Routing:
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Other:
- board size 169.8 x 107.5 mm -> 170 x 110 mm

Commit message: fix: main
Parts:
- added D18: LED_PWR, 0.main.robot:LED_SMLE13WBC8W1, F.Cu at (187.0, 73.0)
- added R43: 470, Resistor_SMD:R_0603_1608Metric_Pad0.98x0.95mm_HandSolder, F.Cu at (191.3, 73.0)
- C10, C12, J10, J11, J6, R11, R15, R19, R22, R23, R4, R9, SW3, U5: moved to B.Cu
- C3, C6, R25, R5, SW2: moved to F.Cu
- J7: footprint 0.main.robot:JSTB4B-ZR -> Connector_PinHeader_2.54mm:PinHeader_1x04_P2.54mm_Vertical; moved to B.Cu
- SW1: footprint Button_Switch_SMD:Panasonic_EVQPUJ_EVQPUA -> 0.main.robot:THAU13-AB-R
- SW4: footprint 0.main.robot:TVAF06-A020B-R -> 0.main.robot:THAU13-AB-R
- moved D4 178.1 mm to (225.0, 85.0)
- moved R5 175.2 mm to (229.0, 91.0)
- moved C1 154.5 mm to (229.0, 80.0), turned to 0 degrees
- moved C11 129.0 mm to (108.0, 116.0), turned to 0 degrees
- moved C10 125.5 mm to (107.0, 120.0), turned to 0 degrees
- moved U7 125.5 mm to (107.0, 120.0)
- moved D8 113.6 mm to (110.1, 132.0)
- moved R20 112.4 mm to (127.1, 135.0)
- moved D6 102.8 mm to (118.1, 129.0), turned to 0 degrees
- moved U5 98.3 mm to (118.1, 129.0), turned to -90 degrees
- moved R25 97.0 mm to (110.0, 128.0)
- moved C5 93.9 mm to (119.1, 136.0), turned to 180 degrees
- moved Y1 93.4 mm to (121.6, 120.0), turned to 180 degrees
- moved R24 92.1 mm to (110.1, 135.0), turned to 180 degrees
- moved R21 87.8 mm to (114.0, 115.0)
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
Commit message: PCB 修正
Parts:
- added G***: LOGO, 0.main.robot:MMA_Logo, F.Cu at (179.7, 62.2)
- added J21: GND-Test, Connector_PinHeader_2.54mm:PinHeader_1x01_P2.54mm_Vertical, F.Cu at (147.3, 136.5)
- D3: value LED -> LED_BUILTIN
- D4: footprint Diode_SMD:D_SMA -> Diode_SMD:D_0805_2012Metric_Pad1.15x1.40mm_HandSolder
- D5: value LED -> 5V
- JP1: footprint Connector_PinHeader_1.27mm:PinHeader_1x02_P1.27mm_Vertical -> Jumper:SolderJumper-2_P1.3mm_Bridged2Bar_RoundedPad1.0x1.5mm
- moved U3 84.6 mm to (122.6, 62.9)
- moved R9 83.9 mm to (116.8, 69.8), turned to -90 degrees
- moved U2 83.5 mm to (118.1, 62.9), turned to 90 degrees
- moved R11 81.8 mm to (113.7, 69.8)
- moved R14 78.5 mm to (125.7, 69.8), turned to -90 degrees
- moved R15 77.3 mm to (120.0, 69.8)
- moved R13 76.0 mm to (122.6, 69.8), turned to -90 degrees
- moved R27 52.1 mm to (99.4, 89.5), turned to 0 degrees
- moved J18 49.0 mm to (108.3, 91.3)
- moved JP1 46.9 mm to (142.9, 136.5)
- moved R28 46.6 mm to (99.4, 93.3), turned to 0 degrees
- moved C12 36.9 mm to (106.0, 109.9)
- moved C6 18.9 mm to (106.3, 129.5), turned to -90 degrees
- moved JP2 13.2 mm to (73.0, 89.5)
- moved C3 9.76 mm to (172.7, 132.1), turned to 90 degrees
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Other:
- board text added: "Ver 1.0 A.Saeki Mar.03.2023"
